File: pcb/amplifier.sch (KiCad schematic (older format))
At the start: 63 parts, among them J2 SMA, J3 SMA, P6 CONN_02X03, Q2 BF861, U10 TPS77001DBVT, U11 AD829, U12 AD8061, U13 AD8031

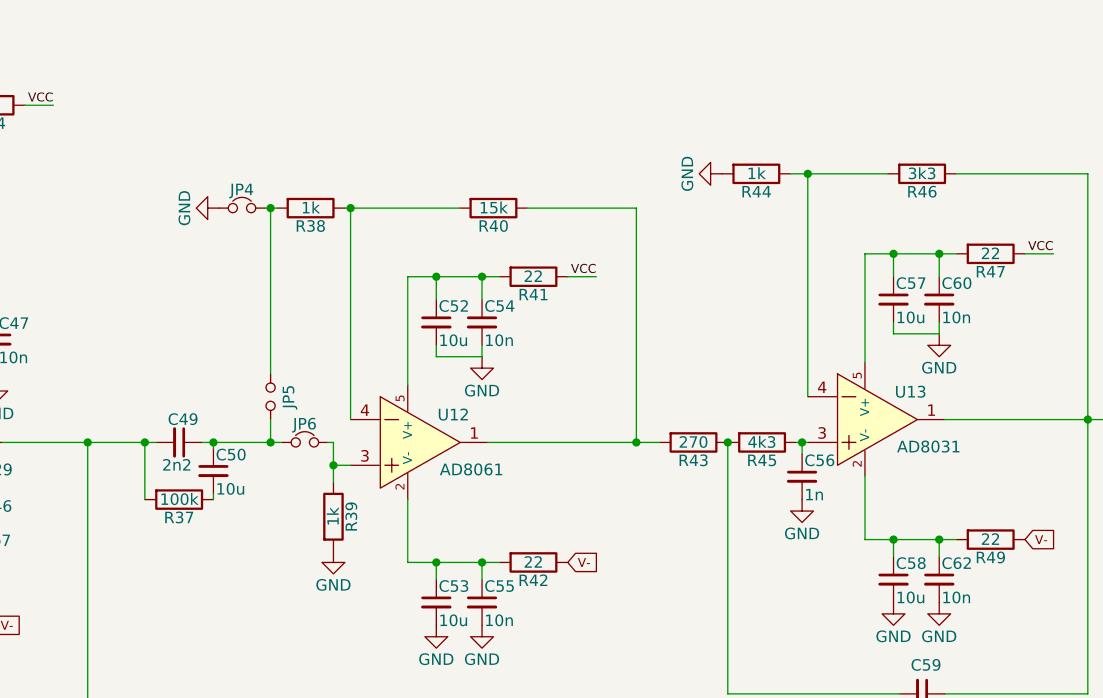
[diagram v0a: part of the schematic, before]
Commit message: pcb: Update to v1.1
Changes:
 Add input protection diodes to acquisition board
 Add second screw hole to the preamplifier
 Add PCB revision number to the board
 LPF->HPF at the output of the preamplifier board
 Fix connector orientation on the preamplifier board
 Fix enclosure front/back PCBs
 Add constant amplification resistor to the acquisition board
 Switch the reference to 2.0V because MAX4477 has low maximal input common mode
 voltage
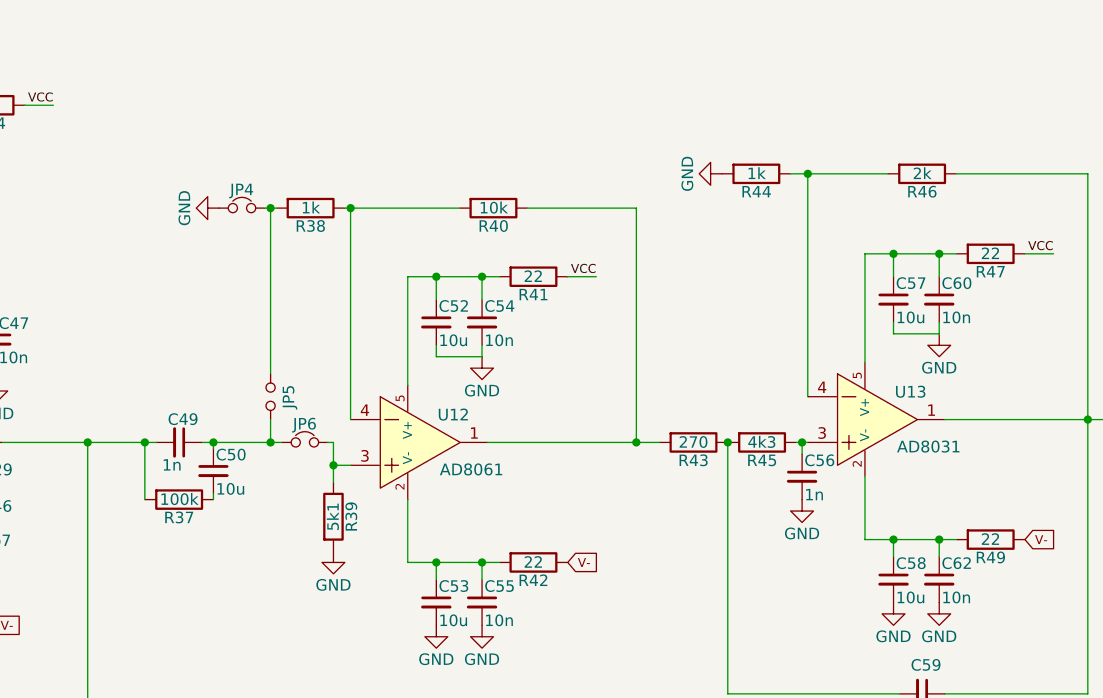
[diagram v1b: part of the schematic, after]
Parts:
- C49: value 2n2 -> 1n
- R39: value 1k -> 5k1
- R40: value 15k -> 10k
- R46: value 3k3 -> 2k
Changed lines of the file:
@@
 Title "Amplifier"
 Date ""
-Rev "1.0"
+Rev "1.1"
 Comp "Institute of Experimental and Applied Physics"
 Comment1 "Based on FITPix amplifier by Milan Petrik (http://dentec.cz)"
@@
 $EndComp
 $Comp
-L GND #PWR068
+L GND #PWR77
 U 1 1 5730DA75
 P 3125 7075
-F 0 "#PWR068" H 3125 6825 50  0001 C CNN
+F 0 "#PWR77" H 3125 6825 50  0001 C CNN
 F 1 "GND" H 3125 6925 50  0000 C CNN
 F 2 "" H 3125 7075 50  0000 C CNN
@@
 $EndComp
 $Comp
-L +5V #PWR069
+L +5V #PWR71
 U 1 1 5730DA91
 P 2025 6700
-F 0 "#PWR069" H 2025 6550 50  0001 C CNN
+F 0 "#PWR71" H 2025 6550 50  0001 C CNN
 F 1 "+5V" H 2025 6840 50  0000 C CNN
 F 2 "" H 2025 6700 50  0000 C CNN
@@
 $EndComp
 $Comp
-L GND #PWR070
+L GND #PWR73
 U 1 1 5730DBDA
 P 2650 6975
-F 0 "#PWR070" H 2650 6725 50  0001 C CNN
+F 0 "#PWR73" H 2650 6725 50  0001 C CNN
 F 1 "GND" H 2650 6825 50  0000 C CNN
 F 2 "" H 2650 6975 50  0000 C CNN
@@
 $EndComp
 $Comp
-L GND #PWR071
+L GND #PWR81
 U 1 1 5730DF3C
 P 3725 7325
-F 0 "#PWR071" H 3725 7075 50  0001 C CNN
+F 0 "#PWR81" H 3725 7075 50  0001 C CNN
 F 1 "GND" H 3725 7175 50  0000 C CNN
 F 2 "" H 3725 7325 50  0000 C CNN
@@
 VCC
 $Comp
-L GND #PWR072
+L GND #PWR82
 U 1 1 5730E917
 P 4000 7275
-F 0 "#PWR072" H 4000 7025 50  0001 C CNN
+F 0 "#PWR82" H 4000 7025 50  0001 C CNN
 F 1 "GND" H 4000 7125 50  0000 C CNN
 F 2 "" H 4000 7275 50  0000 C CNN
@@
 $EndComp
 $Comp
-L GND #PWR073
+L GND #PWR84
 U 1 1 5730ECB1
 P 4650 6975
-F 0 "#PWR073" H 4650 6725 50  0001 C CNN
+F 0 "#PWR84" H 4650 6725 50  0001 C CNN
 F 1 "GND" H 4650 6825 50  0000 C CNN
 F 2 "" H 4650 6975 50  0000 C CNN
@@
 Amplifier
 $Comp
-L GND #PWR074
+L GND #PWR69
 U 1 1 5730F8FA
 P 875 3600
-F 0 "#PWR074" H 875 3350 50  0001 C CNN
+F 0 "#PWR69" H 875 3350 50  0001 C CNN
 F 1 "GND" H 875 3450 50  0000 C CNN
 F 2 "" H 875 3600 50  0000 C CNN
@@
 $EndComp
 $Comp
-L GND #PWR075
+L GND #PWR70
 U 1 1 573102EB
 P 1000 2950
-F 0 "#PWR075" H 1000 2700 50  0001 C CNN
+F 0 "#PWR70" H 1000 2700 50  0001 C CNN
 F 1 "GND" H 1000 2800 50  0000 C CNN
 F 2 "" H 1000 2950 50  0000 C CNN
@@
 $EndComp
 $Comp
-L GND #PWR076
+L GND #PWR72
 U 1 1 57313295
 P 2500 3900
-F 0 "#PWR076" H 2500 3650 50  0001 C CNN
+F 0 "#PWR72" H 2500 3650 50  0001 C CNN
 F 1 "GND" H 2500 3750 50  0000 C CNN
 F 2 "" H 2500 3900 50  0000 C CNN
@@
 $EndComp
 $Comp
-L GND #PWR077
+L GND #PWR79
 U 1 1 57314982
 P 3575 4150
-F 0 "#PWR077" H 3575 3900 50  0001 C CNN
+F 0 "#PWR79" H 3575 3900 50  0001 C CNN
 F 1 "GND" H 3575 4000 50  0000 C CNN
 F 2 "" H 3575 4150 50  0000 C CNN
@@
 $EndComp
 $Comp
-L GND #PWR078
+L GND #PWR75
 U 1 1 57315E76
 P 2950 4175
-F 0 "#PWR078" H 2950 3925 50  0001 C CNN
+F 0 "#PWR75" H 2950 3925 50  0001 C CNN
 F 1 "GND" H 2950 4025 50  0000 C CNN
 F 2 "" H 2950 4175 50  0000 C CNN
@@
 $EndComp
 $Comp
-L GND #PWR079
+L GND #PWR74
 U 1 1 573169F0
 P 2775 4100
-F 0 "#PWR079" H 2775 3850 50  0001 C CNN
+F 0 "#PWR74" H 2775 3850 50  0001 C CNN
 F 1 "GND" H 2775 3950 50  0000 C CNN
 F 2 "" H 2775 4100 50  0000 C CNN
@@
 $EndComp
 $Comp
-L GND #PWR080
+L GND #PWR80
 U 1 1 57318449
 P 3650 3425
-F 0 "#PWR080" H 3650 3175 50  0001 C CNN
+F 0 "#PWR80" H 3650 3175 50  0001 C CNN
 F 1 "GND" H 3650 3275 50  0000 C CNN
 F 2 "" H 3650 3425 50  0000 C CNN
@@
 $EndComp
 $Comp
-L GND #PWR081
+L GND #PWR76
 U 1 1 5731B7AA
 P 2975 4750
-F 0 "#PWR081" H 2975 4500 50  0001 C CNN
+F 0 "#PWR76" H 2975 4500 50  0001 C CNN
 F 1 "GND" H 2975 4600 50  0000 C CNN
 F 2 "" H 2975 4750 50  0000 C CNN
@@
 P 4450 3700
 F 0 "C49" V 4350 3650 50  0000 L CNN
-F 1 "2n2" V 4550 3625 50  0000 L CNN
+F 1 "1n" V 4550 3625 50  0000 L CNN
 F 2 "Resistors_SMD:R_0402" H 4450 3700 50  0001 C CNN
 F 3 "" H 4450 3700 50  0000 C CNN
@@
 P 5125 4025
 F 0 "R39" V 5205 4025 50  0000 C CNN
-F 1 "1k" V 5125 4025 50  0000 C CNN
+F 1 "5k1" V 5125 4025 50  0000 C CNN
 F 2 "Resistors_SMD:R_0402" V 5055 4025 50  0001 C CNN
 F 3 "" H 5125 4025 50  0000 C CNN
@@
 $EndComp
 $Comp
-L GND #PWR082
+L GND #PWR85
 U 1 1 57322AC4
 P 5125 4175
-F 0 "#PWR082" H 5125 3925 50  0001 C CNN
+F 0 "#PWR85" H 5125 3925 50  0001 C CNN
 F 1 "GND" H 5125 4025 50  0000 C CNN
 F 2 "" H 5125 4175 50  0000 C CNN
@@
 P 5825 2675
 F 0 "R40" V 5905 2675 50  0000 C CNN
-F 1 "15k" V 5825 2675 50  0000 C CNN
+F 1 "10k" V 5825 2675 50  0000 C CNN
 F 2 "Resistors_SMD:R_0402" V 5755 2675 50  0001 C CNN
 F 3 "" H 5825 2675 50  0000 C CNN
@@
 $EndComp
 $Comp
-L GND #PWR083
+L GND #PWR83
 U 1 1 57324401
 P 4625 2675
-F 0 "#PWR083" H 4625 2425 50  0001 C CNN
+F 0 "#PWR83" H 4625 2425 50  0001 C CNN
 F 1 "GND" H 4625 2525 50  0000 C CNN
 F 2 "" H 4625 2675 50  0000 C CNN
@@
 $EndComp
 $Comp
-L GND #PWR084
+L GND #PWR78
 U 1 1 57330630
 P 3175 4750
-F 0 "#PWR084" H 3175 4500 50  0001 C CNN
+F 0 "#PWR78" H 3175 4500 50  0001 C CNN
 F 1 "GND" H 3175 4600 50  0000 C CNN
 F 2 "" H 3175 4750 50  0000 C CNN
@@
 $EndComp
 $Comp
-L GND #PWR085
+L GND #PWR87
 U 1 1 57332370
 P 5775 3325
-F 0 "#PWR085" H 5775 3075 50  0001 C CNN
+F 0 "#PWR87" H 5775 3075 50  0001 C CNN
 F 1 "GND" H 5775 3175 50  0000 C CNN
 F 2 "" H 5775 3325 50  0000 C CNN
@@
 $EndComp
 $Comp
-L GND #PWR086
+L GND #PWR86
 U 1 1 5733A90D
 P 5575 4500
-F 0 "#PWR086" H 5575 4250 50  0001 C CNN
+F 0 "#PWR86" H 5575 4250 50  0001 C CNN
 F 1 "GND" H 5575 4350 50  0000 C CNN
 F 2 "" H 5575 4500 50  0000 C CNN
@@
 $EndComp
 $Comp
-L GND #PWR087
+L GND #PWR88
 U 1 1 5733A924
 P 5775 4500
-F 0 "#PWR087" H 5775 4250 50  0001 C CNN
+F 0 "#PWR88" H 5775 4250 50  0001 C CNN
 F 1 "GND" H 5775 4350 50  0000 C CNN
 F 2 "" H 5775 4500 50  0000 C CNN
@@
 $EndComp
 $Comp
-L GND #PWR088
+L GND #PWR94
 U 1 1 57341609
 P 9025 3975
-F 0 "#PWR088" H 9025 3725 50  0001 C CNN
+F 0 "#PWR94" H 9025 3725 50  0001 C CNN
 F 1 "GND" H 9025 3825 50  0000 C CNN
 F 2 "" H 9025 3975 50  0000 C CNN
@@
 $EndComp
 $Comp
-L GND #PWR089
+L GND #PWR95
 U 1 1 57342776
 P 9475 3800
-F 0 "#PWR089" H 9475 3550 50  0001 C CNN
+F 0 "#PWR95" H 9475 3550 50  0001 C CNN
 F 1 "GND" H 9475 3650 50  0000 C CNN
 F 2 "" H 9475 3800 50  0000 C CNN
@@
 $EndComp
 $Comp
-L GND #PWR090
+L GND #PWR96
 U 1 1 57322E60
 P 10100 5300
-F 0 "#PWR090" H 10100 5050 50  0001 C CNN
+F 0 "#PWR96" H 10100 5050 50  0001 C CNN
 F 1 "GND" V 10100 5100 50  0000 C CNN
 F 2 "" H 10100 5300 50  0000 C CNN
@@
 $EndComp
 $Comp
-L +5V #PWR091
+L +5V #PWR97
 U 1 1 57322E66
 P 10100 5500
-F 0 "#PWR091" H 10100 5350 50  0001 C CNN
+F 0 "#PWR97" H 10100 5350 50  0001 C CNN
 F 1 "+5V" V 10100 5700 50  0000 C CNN
 F 2 "" H 10100 5500 50  0000 C CNN
@@
 $EndComp
 $Comp
-L GND #PWR092
+L GND #PWR91
 U 1 1 57344C5F
 P 7575 4400
-F 0 "#PWR092" H 7575 4150 50  0001 C CNN
+F 0 "#PWR91" H 7575 4150 50  0001 C CNN
 F 1 "GND" H 7575 4250 50  0000 C CNN
 F 2 "" H 7575 4400 50  0000 C CNN
@@
 $EndComp
 $Comp
-L GND #PWR093
+L GND #PWR93
 U 1 1 57344C73
 P 7775 4400
-F 0 "#PWR093" H 7775 4150 50  0001 C CNN
+F 0 "#PWR93" H 7775 4150 50  0001 C CNN
 F 1 "GND" H 7775 4250 50  0000 C CNN
 F 2 "" H 7775 4400 50  0000 C CNN
@@
 $EndComp
 $Comp
-L GND #PWR094
+L GND #PWR92
 U 1 1 573450B8
 P 7775 3225
-F 0 "#PWR094" H 7775 2975 50  0001 C CNN
+F 0 "#PWR92" H 7775 2975 50  0001 C CNN
 F 1 "GND" H 7775 3075 50  0000 C CNN
 F 2 "" H 7775 3225 50  0000 C CNN
@@
 P 7700 2525
 F 0 "R46" V 7780 2525 50  0000 C CNN
-F 1 "3k3" V 7700 2525 50  0000 C CNN
+F 1 "2k" V 7700 2525 50  0000 C CNN
 F 2 "Resistors_SMD:R_0402" V 7630 2525 50  0001 C CNN
 F 3 "" H 7700 2525 50  0000 C CNN
@@
 $EndComp
 $Comp
-L GND #PWR095
+L GND #PWR89
 U 1 1 57347ADA
 P 6825 2525
-F 0 "#PWR095" H 6825 2275 50  0001 C CNN
+F 0 "#PWR89" H 6825 2275 50  0001 C CNN
 F 1 "GND" H 6825 2375 50  0000 C CNN
 F 2 "" H 6825 2525 50  0000 C CNN
@@
 Connection ~ 7175 3700
 $Comp
-L GND #PWR096
+L GND #PWR90
 U 1 1 5734ABE2
 P 7175 3950
-F 0 "#PWR096" H 7175 3700 50  0001 C CNN
+F 0 "#PWR90" H 7175 3700 50  0001 C CNN
 F 1 "GND" H 7175 3800 50  0000 C CNN
 F 2 "" H 7175 3950 50  0000 C CNN

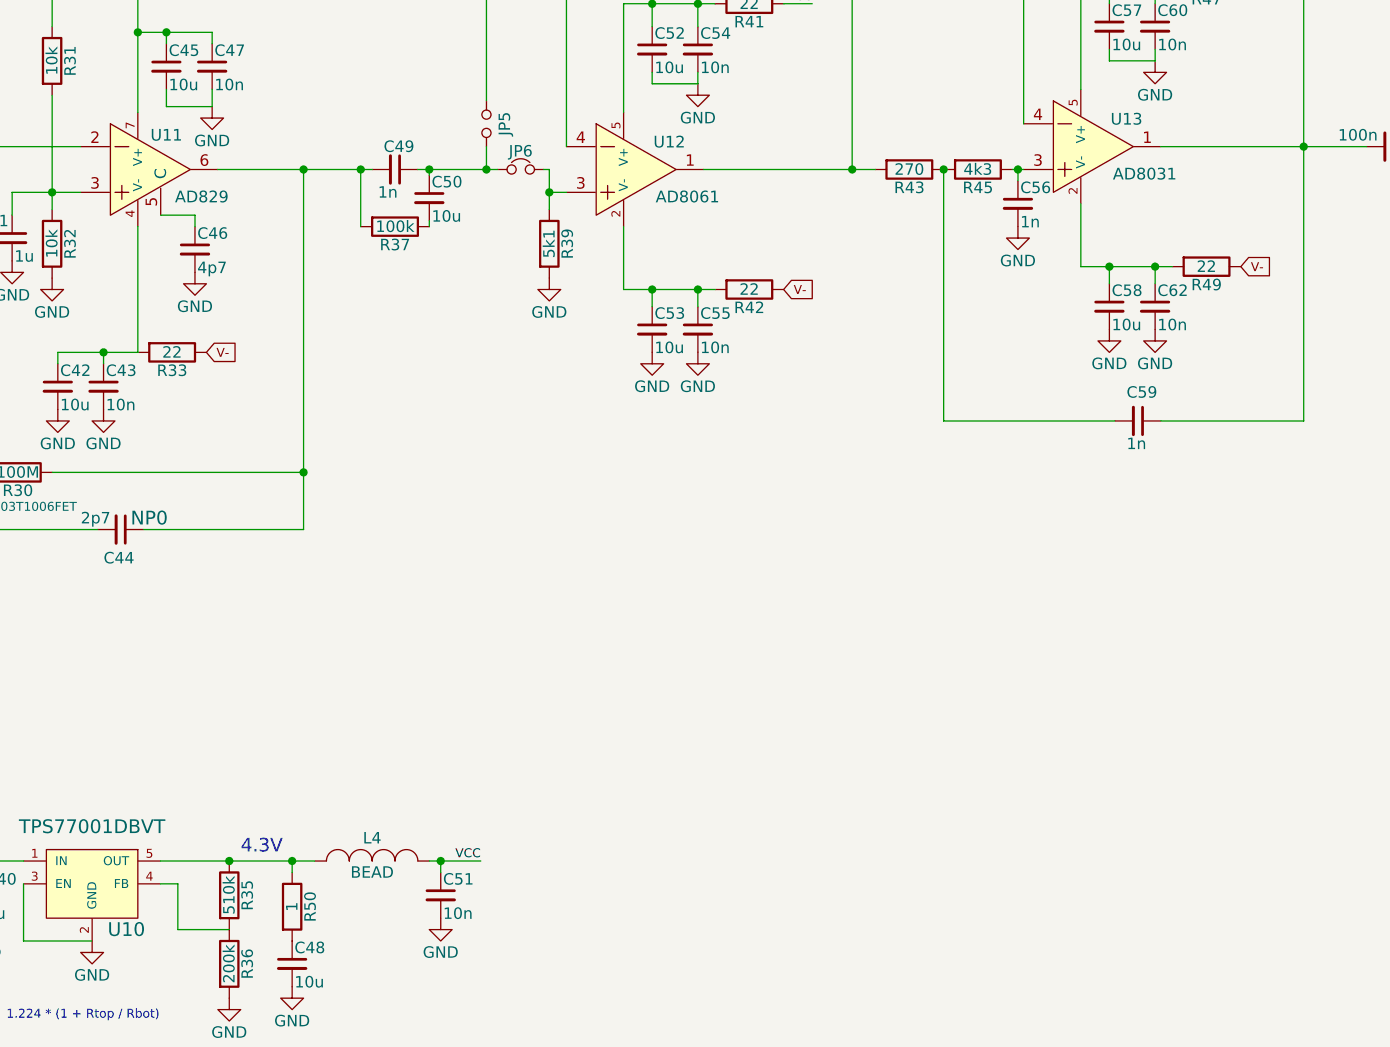
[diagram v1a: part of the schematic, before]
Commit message: pcb: Update to the current iteration
Looks like I forgot to commit the changes made for manufacturing...
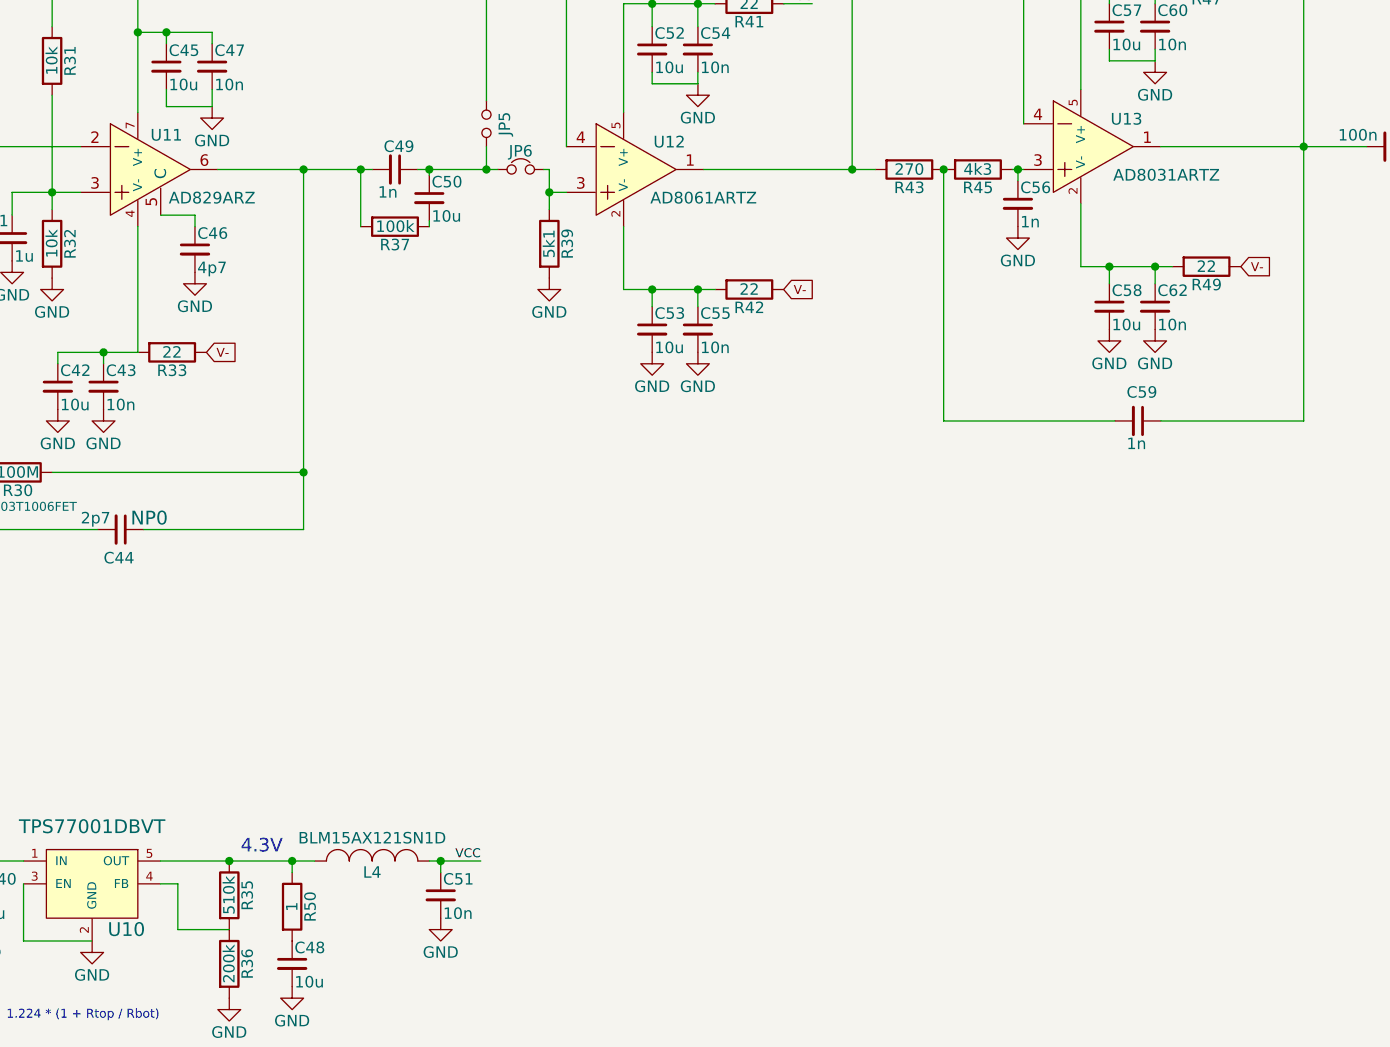
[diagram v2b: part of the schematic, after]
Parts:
- JP4, JP6: value Jumper_NC_Small -> 0R
- JP5: value Jumper_NO_Small -> DNP
- L4: value BEAD -> BLM15AX121SN1D
- U11: value AD829 -> AD829ARZ
- U12: value AD8061 -> AD8061ARTZ
- U13: value AD8031 -> AD8031ARTZ
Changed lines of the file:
@@
 EESchema Schematic File Version 2
+LIBS:pcb-rescue
 LIBS:power
 LIBS:device
@@
 U 1 1 5730E9FE
 P 4350 6725
-F 0 "L4" H 4350 6825 50  0000 C CNN
-F 1 "BEAD" H 4350 6675 50  0000 C CNN
+F 0 "L4" H 4350 6675 50  0000 C CNN
+F 1 "BLM15AX121SN1D" H 4350 6825 50  0000 C CNN
 F 2 "Resistors_SMD:R_0402" H 4350 6725 50  0001 C CNN
 F 3 "" H 4350 6725 50  0000 C CNN
@@
 P 3325 3700
 F 0 "U11" H 3450 3850 51  0000 C CNN
-F 1 "AD829" H 3605 3580 51  0000 C CNN
+F 1 "AD829ARZ" H 3650 3575 51  0000 C CNN
 F 2 "Housings_SOIC:SOIC-8_3.9x4.9mm_Pitch1.27mm" H 3215 3300 157 0001 C CNN
 F 3 "" H 3215 3300 157 0000 C CNN
@@
 P 5450 3700
 F 0 "U12" H 5650 3820 51  0000 C CNN
-F 1 "AD8061" H 5730 3580 51  0000 C CNN
+F 1 "AD8061ARTZ" H 5800 3575 51  0000 C CNN
 F 2 "TO_SOT_Packages_SMD:SOT-23-5" H 5340 3300 157 0001 C CNN
 F 3 "" H 5340 3300 157 0000 C CNN
@@
 P 4725 2675
 F 0 "JP4" H 4725 2755 50  0000 C CNN
-F 1 "Jumper_NC_Small" H 4735 2615 50  0001 C CNN
+F 1 "0R" H 4735 2615 50  0001 C CNN
 F 2 "Resistors_SMD:R_0402" H 4725 2675 50  0001 C CNN
 F 3 "" H 4725 2675 50  0000 C CNN
@@
 P 4850 3500
 F 0 "JP5" H 4850 3580 50  0000 C CNN
-F 1 "Jumper_NO_Small" H 4860 3440 50  0001 C CNN
+F 1 "DNP" H 4860 3440 50  0001 C CNN
 F 2 "Resistors_SMD:R_0402" H 4850 3500 50  0001 C CNN
 F 3 "" H 4850 3500 50  0000 C CNN
@@
 P 5000 3700
 F 0 "JP6" H 5000 3780 50  0000 C CNN
-F 1 "Jumper_NC_Small" H 5010 3640 50  0001 C CNN
+F 1 "0R" H 5010 3640 50  0001 C CNN
 F 2 "Resistors_SMD:R_0402" H 5000 3700 50  0001 C CNN
 F 3 "" H 5000 3700 50  0000 C CNN
@@
 P 7450 3600
 F 0 "U13" H 7650 3720 51  0000 C CNN
-F 1 "AD8031" H 7730 3480 51  0000 C CNN
+F 1 "AD8031ARTZ" H 7825 3475 51  0000 C CNN
 F 2 "TO_SOT_Packages_SMD:SOT-23-5" H 7340 3200 157 0001 C CNN
 F 3 "" H 7340 3200 157 0000 C CNN
